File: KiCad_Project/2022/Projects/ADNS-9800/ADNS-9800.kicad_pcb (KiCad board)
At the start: 2 copper layers, 31.5 x 31.5 mm, 15 parts, among them Q1 TRANSISTOR_SC-75

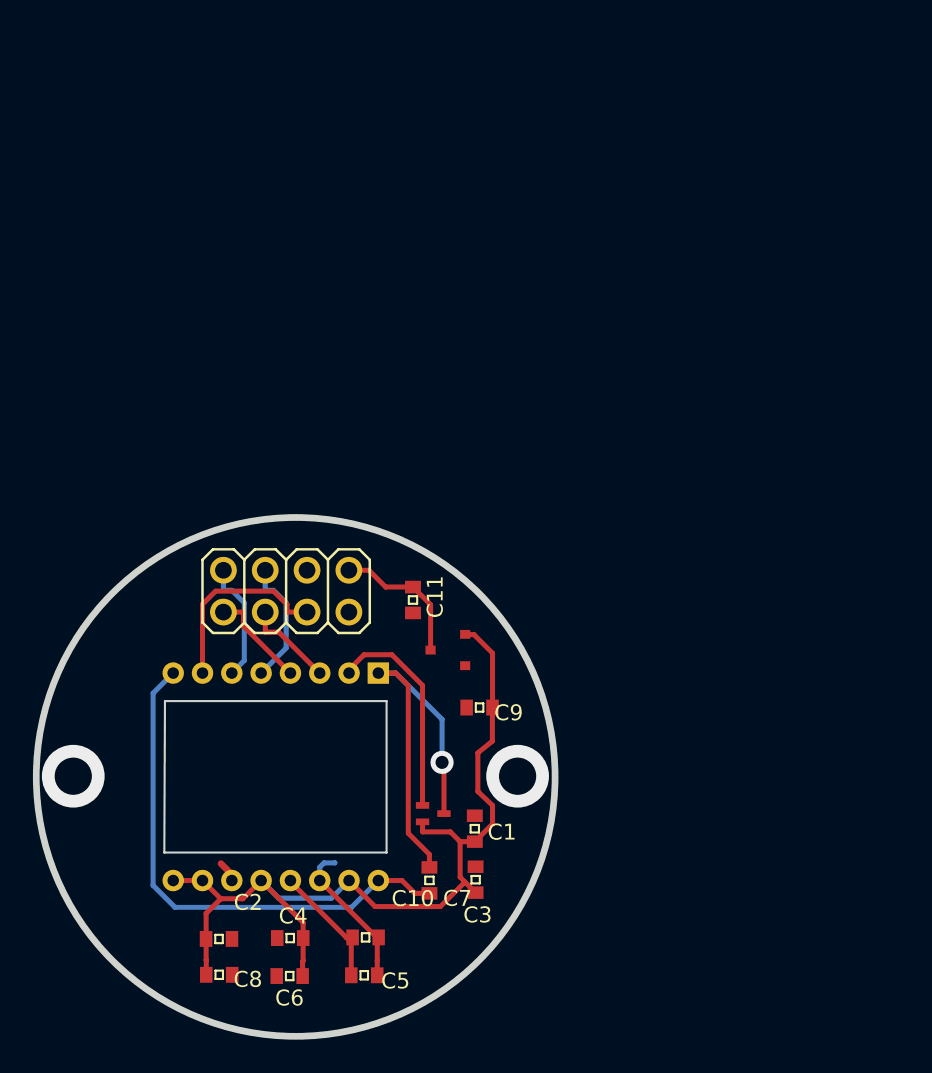
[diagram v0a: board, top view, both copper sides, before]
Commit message: マウスセンサの設計の完了
ADNS－9800使用
SeeeduinoXIAOを用いてUARTでメインマイコンと通信
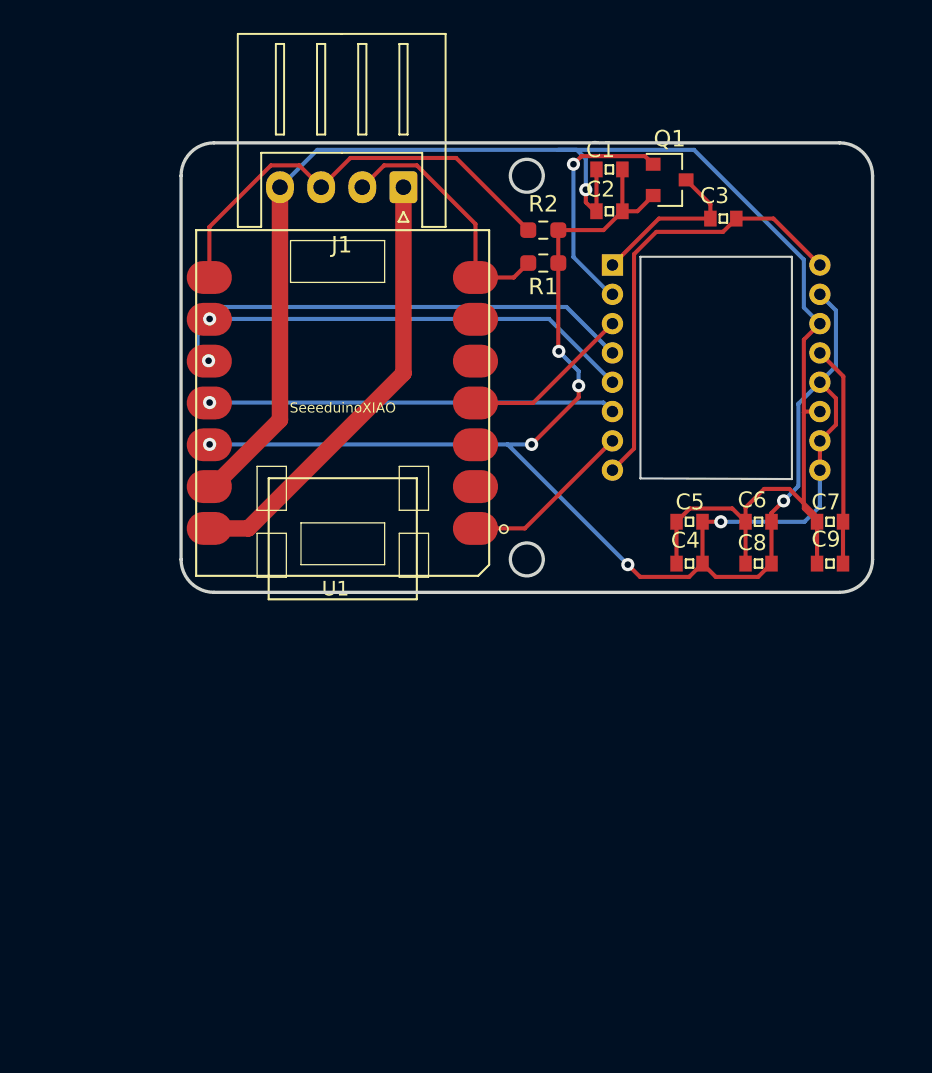
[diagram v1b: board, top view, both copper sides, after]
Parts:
- removed C11: 1uF, ADNS-9800:0603
- removed the C9 at (159.6, 100.8)
- removed JP1: PINHD-2X4, ADNS-9800:2X04
- removed U$2: MCP1700__LDO, ADNS-9800:MCP1700__LDO
- added J1: Conn_01x04, Connector_JST:JST_XH_S4B-XH-A_1x04_P2.50mm_Horizontal, F.Cu at (155.0, 69.2)
- added R1: R, Resistor_SMD:R_0603_1608Metric_Pad0.98x0.95mm_HandSolder, F.Cu at (163.5, 73.8)
- added R2: R, Resistor_SMD:R_0603_1608Metric_Pad0.98x0.95mm_HandSolder, F.Cu at (163.5, 71.8)
- added U1: SeeeduinoXIAO, Library:Seeeduino XIAO-MOUDLE14P-2.54-21X17.8MM, F.Cu at (160.2, 71.8)
- Q1: value TRANSISTOR_SC-75 -> IRLML6402; footprint ADNS-9800:SC-75_TRANSISTOR -> Package_TO_SOT_SMD:SOT-23
- moved C3 44.0 mm to (174.4, 71.1), turned to 180 degrees
- moved C1 43.9 mm to (167.5, 68.1), turned to 0 degrees
- moved Q1 40.8 mm to (171.2, 68.7), turned to 0 degrees
- moved C2 38.4 mm to (167.5, 70.7), turned to 0 degrees
- moved C5 38.2 mm to (172.4, 89.5), turned to 0 degrees
- moved C6 38.1 mm to (176.6, 89.5)
- moved C4 37.9 mm to (172.4, 92.1), turned to 0 degrees
- moved C8 37.9 mm to (176.6, 92.1)
- moved C7 37.9 mm to (180.9, 89.5), turned to 0 degrees
- moved C9 37.8 mm to (180.9, 92.1), turned to 0 degrees
- moved U$1 28.6 mm to (167.7, 73.9), turned to 90 degrees
- renumbered C3 to C1, C1 to C2, C7 to C3, C8 to C4, C2 to C5, C4 to C6, C10 to C7, C6 to C8, C5 to C9
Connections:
- net /VREG renamed +3V3
- C1 pad 1: /AGND -> GND
- C2 pad 1: /AGND -> GND
- C4 pad 1: /AGND -> GND
- C5 pad 1: /AGND -> GND
- C6 pad 1: /AGND -> GND
- C7 pad 1: /DGND -> GND
- C8 pad 1: /AGND -> GND
- C9 pad 1: /DGND -> GND
- U$1 pad P$11: /AGND -> GND
- U$1 pad P$14: /DGND -> GND
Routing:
- net GND: track 0.00 -> 100.8 mm, vias 0 -> 1
- net +3V3: track 55.0 -> 100.6 mm, vias 0 -> 7
- net RX: track 0.00 -> 27.1 mm
- net +5V: track 0.00 -> 27.0 mm
- net /MISO: track 6.11 -> 29.7 mm, vias 0 -> 1
- net /SCLK: track 7.70 -> 26.1 mm, vias 0 -> 1
- net /MOSI: track 7.38 -> 24.7 mm, vias 0 -> 1
- net TX: track 0.00 -> 15.7 mm
- net Net-(C3-Pad2): track 24.5 -> 10.1 mm, vias 1 -> 0
- net /DGND: track 9.15 -> 0.00 mm
- net /VIN: track 8.59 -> 0.00 mm
- net /REFA: track 7.68 -> 13.4 mm
- net /SS: track 5.56 -> 10.3 mm
- net Net-(C3-Pad1): track 31.7 -> 27.0 mm
- net /AGND: track 1.30 -> 0.00 mm
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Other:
- board size 31.5 x 31.5 mm -> 42 x 27.3 mm
- board text removed: "AG"
- board text removed: "DG"
- board text removed: "MI"
- board text removed: "MO"
- board text removed: "MOT"
- board text removed: "SC"
- board text removed: "SS"
- board text removed: "VI"

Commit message: マウス基板の改良
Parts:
- removed R1, R2: R, Resistor_SMD:R_0603_1608Metric_Pad0.98x0.95mm_HandSolder
- U1: footprint Library:Seeeduino XIAO-MOUDLE14P-2.54-21X17.8MM -> Library:seeeduinoXIAO
- moved U1 14.7 mm to (150.8, 83.0), turned to 0 degrees
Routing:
- net GND: track 100.8 -> 0.00 mm, vias 1 -> 0
- net +5V: track 27.0 -> 0.00 mm
- net +3V3: track 100.6 -> 75.7 mm, vias 7 -> 0
- net Net-(C3-Pad1): track 27.0 -> 6.24 mm
- net RX: track 27.1 -> 9.87 mm
- net /LSR_NEN: track 14.2 -> 0.00 mm, vias 1 -> 0
- net TX: track 15.7 -> 8.67 mm
- net /MISO: track 29.7 -> 26.0 mm
- net /SS: track 10.3 -> 13.3 mm, vias 0 -> 1
- net /MOTION: track 10.5 -> 11.8 mm
- net /MOSI: track 24.7 -> 25.6 mm, vias 1 -> 0
- net /SCLK: track 26.1 -> 25.8 mm, vias 1 -> 0
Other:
- net class Default removed

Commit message: 徹夜の進捗、朝マック食べに行きます
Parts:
- moved U$1 11.4 mm to (179.1, 73.8), turned to 0 degrees
- moved Q1 8.42 mm to (179.5, 69.7)
- moved C1 8.13 mm to (175.5, 69.8), turned to -90 degrees
- moved C7 8.01 mm to (173.0, 88.5)
- moved C9 8.01 mm to (173.0, 91.1)
- moved C3 7.94 mm to (181.6, 74.6), turned to 90 degrees
- moved C2 5.49 mm to (172.9, 69.8), turned to -90 degrees
- moved C4 5.36 mm to (168.3, 88.5), turned to 180 degrees
- moved C5 4.33 mm to (168.3, 91.1), turned to 180 degrees
- moved C6 1.34 mm to (177.5, 88.5)
- moved C8 1.34 mm to (177.5, 91.1)
- moved U1 0.31 mm to (151.1, 82.9)
- moved J1 0.14 mm to (154.9, 69.2)
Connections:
- U1 pad 2: Net-(U1-Pad2) -> unconnected-(U1-Pad2)
- U1 pad 3: Net-(U1-Pad3) -> unconnected-(U1-Pad3)
- U1 pad 5: Net-(U1-Pad5) -> unconnected-(U1-Pad5)
- U1 pad 6: Net-(U1-Pad6) -> unconnected-(U1-Pad6)
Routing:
- net +5V: track 0.00 -> 34.0 mm
- net Net-(C3-Pad1): track 6.24 -> 27.7 mm, vias 0 -> 1
- net +3V3: track 75.7 -> 96.0 mm, vias 0 -> 2
- net /MISO: track 26.0 -> 37.7 mm, vias 1 -> 0
- net /MOTION: track 11.8 -> 23.5 mm, vias 0 -> 1
- net /SS: track 13.3 -> 23.7 mm
- net /REFA: track 13.4 -> 6.17 mm
- net /LSR_NEN: track 0.00 -> 6.19 mm
- net /SCLK: track 25.8 -> 31.0 mm
- net /MOSI: track 25.6 -> 30.5 mm
- net Net-(C3-Pad2): track 10.1 -> 7.01 mm
- net GND: track 0.00 -> 2.62 mm, vias 0 -> 28
- net RX: track 9.87 -> 8.93 mm
- added copper zone on B.Cu, net GND
- added copper zone on F.Cu, net GND
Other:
- board text added: "MUNAKO Hercules ADNS-9800 Mouse_Module ver.2022 Designed by Kiyo"
